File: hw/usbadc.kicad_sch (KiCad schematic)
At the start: 3 parts, among them J4 JTAG

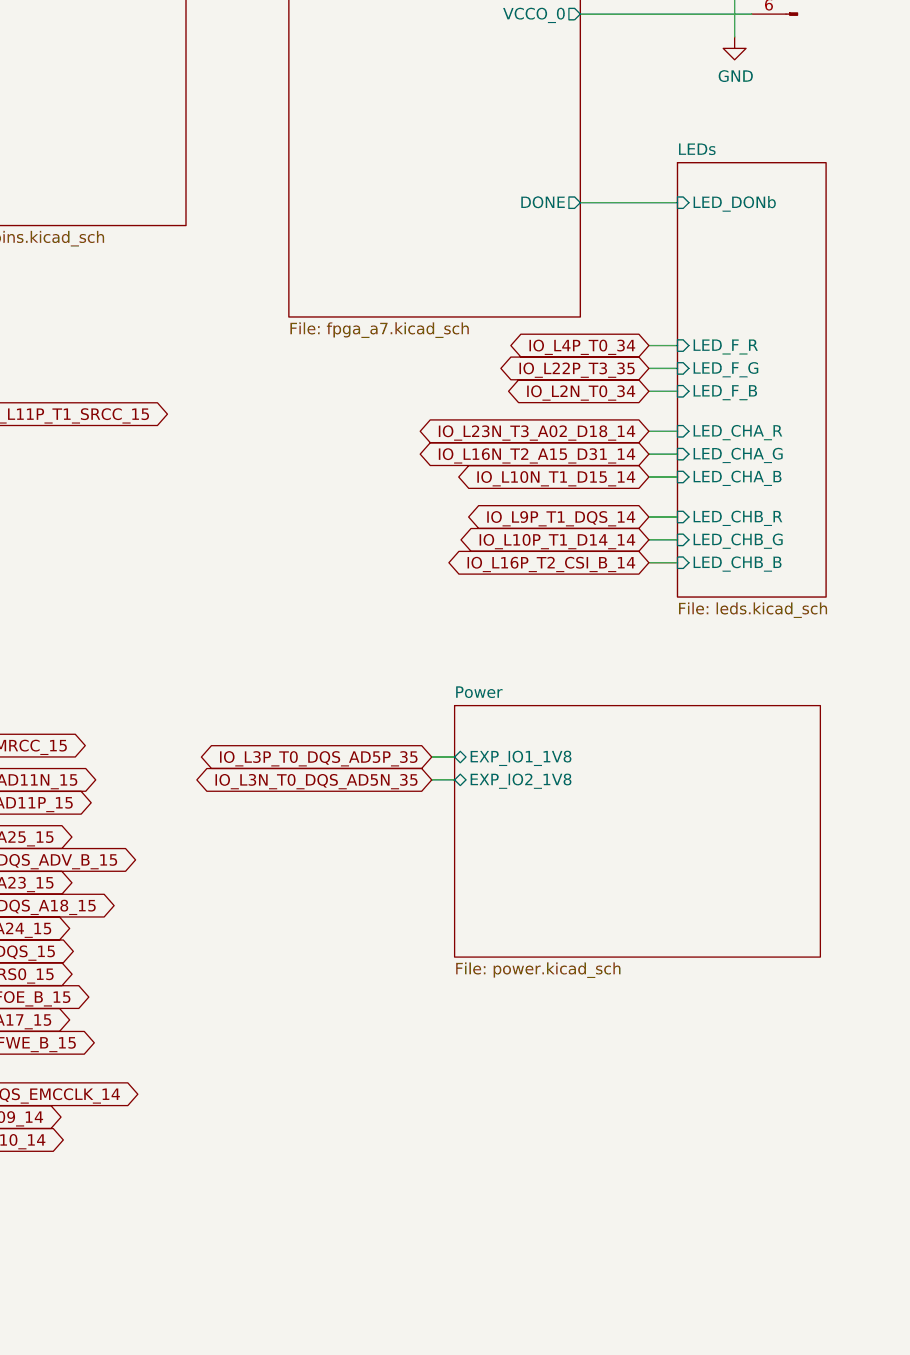
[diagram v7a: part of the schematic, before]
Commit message: added 2nd front led; more keepouts around signal lines
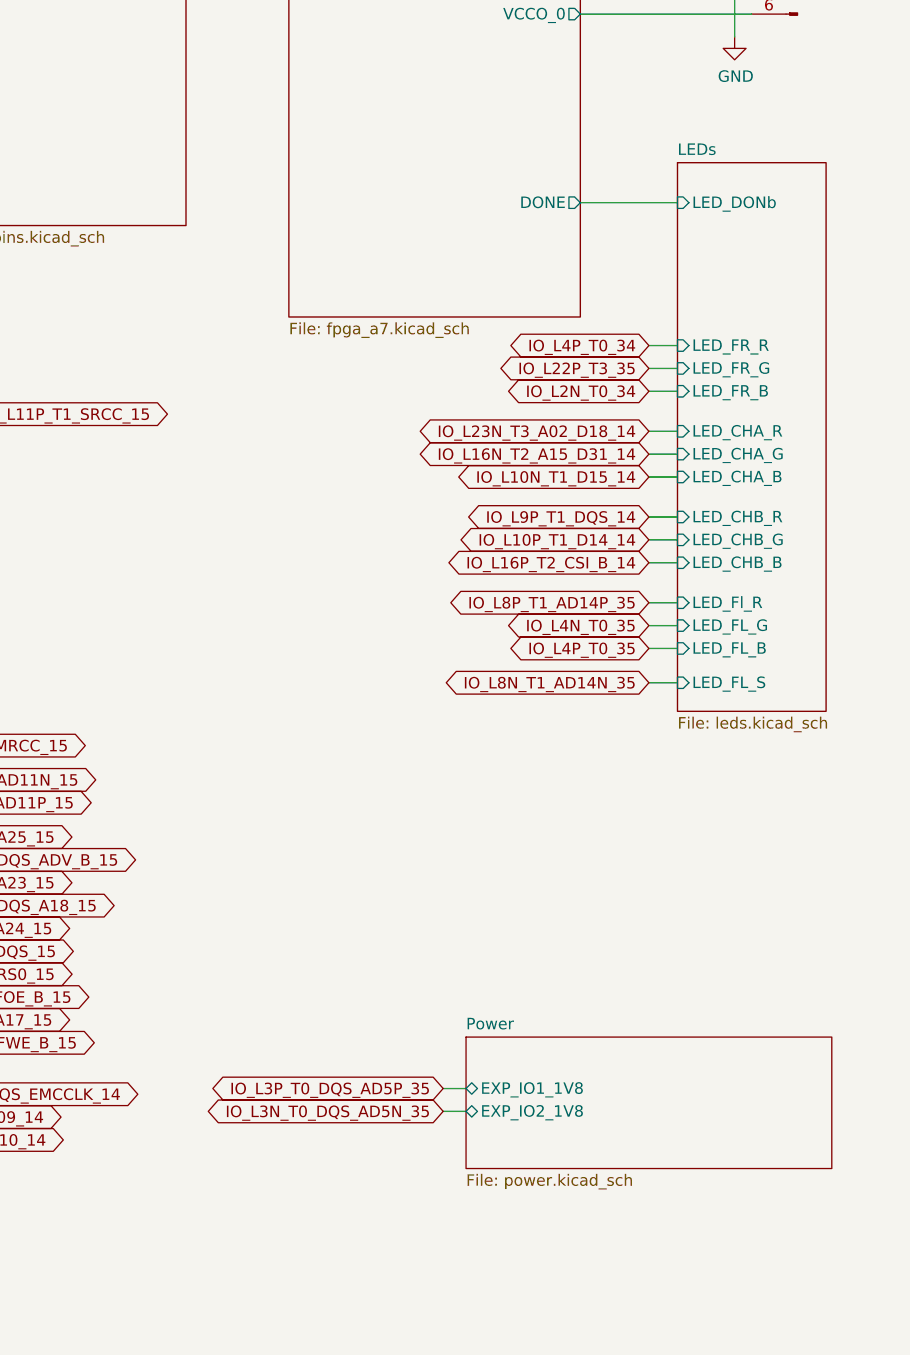
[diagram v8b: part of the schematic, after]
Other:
- sheet LEDs ports: added LED_FL_B, LED_FL_G, LED_FL_S, LED_FR_B, LED_FR_G, LED_FR_R, LED_Fl_R; removed LED_F_B, LED_F_G, LED_F_R
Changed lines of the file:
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@@
+    (stroke (width 0) (type default))
+  )
+  (wire (pts (xy 255.905 107.95) (xy 259.08 107.95))
     (stroke (width 0) (type default))
   )
@@
     (stroke (width 0) (type default))
   )
+  (wire (pts (xy 255.905 104.14) (xy 259.08 104.14))
+    (stroke (width 0) (type default))
+  )
   (wire (pts (xy 265.43 31.115) (xy 265.43 36.195))
     (stroke (width 0) (type default))
@@
     (stroke (width 0) (type default))
   )
-  (wire (pts (xy 231.775 118.745) (xy 234.315 118.745))
+  (wire (pts (xy 233.045 155.575) (xy 235.585 155.575))
     (stroke (width 0) (type default))
   )
@@
     (stroke (width 0) (type default))
   )
+  (wire (pts (xy 255.905 99.06) (xy 259.08 99.06))
+    (stroke (width 0) (type default))
+  )
   (wire (pts (xy 50.165 91.44) (xy 52.705 91.44))
     (stroke (width 0) (type default))
@@
     (stroke (width 0) (type default))
   )
-  (wire (pts (xy 231.775 116.205) (xy 234.315 116.205))
+  (wire (pts (xy 233.045 153.035) (xy 235.585 153.035))
     (stroke (width 0) (type default))
   )
@@
   )
   (wire (pts (xy 50.165 121.92) (xy 52.705 121.92))
+    (stroke (width 0) (type default))
+  )
+  (wire (pts (xy 255.905 101.6) (xy 259.08 101.6))
     (stroke (width 0) (type default))
   )
@@
     )
   )
+  (global_label "IO_L4N_T0_35" (shape bidirectional) (at 255.905 101.6 180) (fields_autoplaced)
+    (effects (font (size 1.27 1.27)) (justify right))
+    (property "Intersheetrefs" "${INTERSHEET_REFS}" (at 239.6986 101.6 0)
+      (effects (font (size 1.27 1.27)) (justify right) hide)
+    )
+  )
   (global_label "IO_L9N_T1_DQS_AD7N_35" (shape bidirectional) (at 50.165 99.06 180) (fields_autoplaced)
     (effects (font (size 1.27 1.27)) (justify right))
@@
     )
   )
-  (global_label "IO_L3N_T0_DQS_AD5N_35" (shape bidirectional) (at 231.775 118.745 180) (fields_autoplaced)
-    (effects (font (size 1.27 1.27)) (justify right))
-    (property "Intersheetrefs" "${INTERSHEET_REFS}" (at 204.9248 118.745 0)
+  (global_label "IO_L3N_T0_DQS_AD5N_35" (shape bidirectional) (at 233.045 155.575 180) (fields_autoplaced)
+    (effects (font (size 1.27 1.27)) (justify right))
+    (property "Intersheetrefs" "${INTERSHEET_REFS}" (at 206.1948 155.575 0)
       (effects (font (size 1.27 1.27)) (justify right) hide)
     )
@@
     )
   )
-  (global_label "IO_L3P_T0_DQS_AD5P_35" (shape bidirectional) (at 231.775 116.205 180) (fields_autoplaced)
-    (effects (font (size 1.27 1.27)) (justify right))
-    (property "Intersheetrefs" "${INTERSHEET_REFS}" (at 205.0458 116.205 0)
+  (global_label "IO_L3P_T0_DQS_AD5P_35" (shape bidirectional) (at 233.045 153.035 180) (fields_autoplaced)
+    (effects (font (size 1.27 1.27)) (justify right))
+    (property "Intersheetrefs" "${INTERSHEET_REFS}" (at 206.3158 153.035 0)
       (effects (font (size 1.27 1.27)) (justify right) hide)
     )
@@
     )
   )
+  (global_label "IO_L4P_T0_35" (shape bidirectional) (at 255.905 104.14 180) (fields_autoplaced)
+    (effects (font (size 1.27 1.27)) (justify right))
+    (property "Intersheetrefs" "${INTERSHEET_REFS}" (at 239.7591 104.14 0)
+      (effects (font (size 1.27 1.27)) (justify right) hide)
+    )
+  )
   (global_label "IO_L8P_T1_D11_14" (shape bidirectional) (at 50.165 127 180) (fields_autoplaced)
     (effects (font (size 1.27 1.27)) (justify right))
@@
     )
   )
+  (global_label "IO_L8N_T1_AD14N_35" (shape bidirectional) (at 255.905 107.95 180) (fields_autoplaced)
+    (effects (font (size 1.27 1.27)) (justify right))
+    (property "Intersheetrefs" "${INTERSHEET_REFS}" (at 232.6229 107.95 0)
+      (effects (font (size 1.27 1.27)) (justify right) hide)
+    )
+  )
   (global_label "IO_L15N_T2_DQS_ADV_B_15" (shape bidirectional) (at 170.815 127.635 0) (fields_autoplaced)
     (effects (font (size 1.27 1.27)) (justify left))
@@
     (property "Intersheetrefs" "${INTERSHEET_REFS}" (at 191.678 158.75 0)
       (effects (font (size 1.27 1.27)) (justify left) hide)
+    )
+  )
+  (global_label "IO_L8P_T1_AD14P_35" (shape bidirectional) (at 255.905 99.06 180) (fields_autoplaced)
+    (effects (font (size 1.27 1.27)) (justify right))
+    (property "Intersheetrefs" "${INTERSHEET_REFS}" (at 232.7439 99.06 0)
+      (effects (font (size 1.27 1.27)) (justify right) hide)
     )
   )
@@
     )
   )
-  (sheet (at 234.315 110.49) (size 40.64 27.94) (fields_autoplaced)
+  (sheet (at 235.585 147.32) (size 40.64 14.605) (fields_autoplaced)
     (stroke (width 0) (type solid))
     (fill (color 0 0 0 0.0000))
-    (property "Sheetname" "Power" (at 234.315 109.7784 0)
+    (property "Sheetname" "Power" (at 235.585 146.6084 0)
       (effects (font (size 1.27 1.27)) (justify left bottom))
     )
-    (property "Sheetfile" "power.kicad_sch" (at 234.315 139.0146 0)
+    (property "Sheetfile" "power.kicad_sch" (at 235.585 162.5096 0)
       (effects (font (size 1.27 1.27)) (justify left top))
     )
-    (pin "EXP_IO1_1V8" bidirectional (at 234.315 116.205 180)
-      (effects (font (size 1.27 1.27)) (justify left))
-    )
-    (pin "EXP_IO2_1V8" bidirectional (at 234.315 118.745 180)
+    (pin "EXP_IO1_1V8" bidirectional (at 235.585 153.035 180)
+      (effects (font (size 1.27 1.27)) (justify left))
+    )
+    (pin "EXP_IO2_1V8" bidirectional (at 235.585 155.575 180)
       (effects (font (size 1.27 1.27)) (justify left))
     )
@@
     )
   )
-  (sheet (at 259.08 50.165) (size 16.51 48.26) (fields_autoplaced)
+  (sheet (at 259.08 50.165) (size 16.51 60.96) (fields_autoplaced)
     (stroke (width 0.1524) (type solid))
     (fill (color 0 0 0 0.0000))
@@
       (effects (font (size 1.27 1.27)) (justify left bottom))
     )
-    (property "Sheetfile" "leds.kicad_sch" (at 259.08 99.0096 0)
+    (property "Sheetfile" "leds.kicad_sch" (at 259.08 111.7096 0)
       (effects (font (size 1.27 1.27)) (justify left top))
     )
@@
       (effects (font (size 1.27 1.27)) (justify left))
     )
-    (pin "LED_F_R" input (at 259.08 70.485 180)
-      (effects (font (size 1.27 1.27)) (justify left))
-    )
-    (pin "LED_F_G" input (at 259.08 73.025 180)
-      (effects (font (size 1.27 1.27)) (justify left))
-    )
-    (pin "LED_F_B" input (at 259.08 75.565 180)
-      (effects (font (size 1.27 1.27)) (justify left))
-    )
     (pin "LED_CHB_B" input (at 259.08 94.615 180)
       (effects (font (size 1.27 1.27)) (justify left))
@@
       (effects (font (size 1.27 1.27)) (justify left))
     )
+    (pin "LED_FR_B" input (at 259.08 75.565 180)
+      (effects (font (size 1.27 1.27)) (justify left))
+    )
+    (pin "LED_FR_G" input (at 259.08 73.025 180)
+      (effects (font (size 1.27 1.27)) (justify left))
+    )
+    (pin "LED_FR_R" input (at 259.08 70.485 180)
+      (effects (font (size 1.27 1.27)) (justify left))
+    )
+    (pin "LED_FL_G" input (at 259.08 101.6 180)
+      (effects (font (size 1.27 1.27)) (justify left))
+    )
+    (pin "LED_FL_B" input (at 259.08 104.14 180)
+      (effects (font (size 1.27 1.27)) (justify left))
+    )
+    (pin "LED_Fl_R" input (at 259.08 99.06 180)
+      (effects (font (size 1.27 1.27)) (justify left))
+    )
+    (pin "LED_FL_S" input (at 259.08 107.95 180)
+      (effects (font (size 1.27 1.27)) (justify left))
+    )
